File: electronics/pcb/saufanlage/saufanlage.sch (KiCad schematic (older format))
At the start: 36 parts

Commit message: Backup commit
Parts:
- removed C? (x4): C, symbol Device:C
- removed D?: D_Schottky, symbol Device:D_Schottky
- removed J?: Conn_02x20_Odd_Even, symbol Connector_Generic:Conn_02x20_Odd_Even
- removed J?: Screw_Terminal_01x02, symbol Connector:Screw_Terminal_01x02
- removed J? (x4): Conn_01x03_Male, symbol Connector:Conn_01x03_Male
- removed J?: Conn_01x02_Female, symbol Connector:Conn_01x02_Female
- removed J?: Conn_01x05_Male, symbol Connector:Conn_01x05_Male
- removed L?: L, symbol Device:L
- removed R? (x6): R, symbol Device:R
- removed SW?: SW_Push, symbol Switch:SW_Push
- removed U?: BD9G341EFJ, Package_SO:HTSOP-8-1EP_3.9x4.9mm_P1.27mm_EP2.4x3.2mm_ThermalVias, symbol Regulator_Switching:BD9G341EFJ
- added J1, J10, J11, J12, J16, J17, J3, J4: Conn_01x08_Male, Connector_PinHeader_2.54mm:PinHeader_1x08_P2.54mm_Vertical, symbol Connector:Conn_01x08_Male
- added J13: Conn_02x03_Odd_Even, Connector_PinHeader_2.54mm:PinHeader_2x03_P2.54mm_Vertical, symbol Connector_Generic:Conn_02x03_Odd_Even
- added J14: Conn_02x18_Odd_Even, Connector_PinHeader_2.54mm:PinHeader_2x18_P2.54mm_Vertical, symbol Connector_Generic:Conn_02x18_Odd_Even
- added J15, J27: Conn_01x10_Male, Connector_PinHeader_2.54mm:PinHeader_1x10_P2.54mm_Vertical, symbol Connector:Conn_01x10_Male
- added J18: Conn_01x04, Connector_PinHeader_2.54mm:PinHeader_1x04_P2.54mm_Vertical, symbol Connector_Generic:Conn_01x04
- added J2: Screw_Terminal_01x02, Connector_Phoenix_MC:PhoenixContact_MCV_1,5_2-G-3.81_1x02_P3.81mm_Vertical, symbol Connector:Screw_Terminal_01x02
- added J23, J24, J29, J30, J31, J32: Conn_01x15_Male, Connector_PinHeader_2.54mm:PinHeader_1x15_P2.54mm_Vertical, symbol Connector:Conn_01x15_Male
- added J7, J9: Conn_01x20_Male, Connector_PinHeader_2.54mm:PinHeader_1x20_P2.54mm_Vertical, symbol Connector:Conn_01x20_Male
- added PS1, PS2: LM2596, saufanlage:LM2596, symbol saufanlage:LM2596
- J19: renamed from J?; footprint (none) -> Connector_PinHeader_2.54mm:PinHeader_1x06_P2.54mm_Vertical
- J20: renamed from J?; footprint (none) -> Connector_PinHeader_2.54mm:PinHeader_1x07_P2.54mm_Vertical
- J21, J25, J26, J28: renamed from J?; footprint (none) -> Connector_PinHeader_2.54mm:PinHeader_1x03_P2.54mm_Vertical
- J22: renamed from J?; footprint (none) -> Connector_PinHeader_2.54mm:PinHeader_1x10_P2.54mm_Vertical
- J5, J6: renamed from J?; footprint (none) -> Connector_PinHeader_2.54mm:PinHeader_2x08_P2.54mm_Vertical
- J8: renamed from J?; footprint (none) -> Connector_PinHeader_2.54mm:PinHeader_2x20_P2.54mm_Vertical
- XA1: renamed from XA?; footprint (none) -> Arduino:Arduino_Mega2560_Shield
- XA2, XA3, XA4: renamed from XA?; footprint (none) -> Arduino:Arduino_Nano_Socket
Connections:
- net labels added: +3.3V, +3V3, +5V, +8V, DT1, DT2, DT3, DT4, Fingerprint, Flowmeter1, Flowmeter2, Flowmeter3, Flowmeter4, MEGA_D20_SDA, MEGA_D21_SCL, MEGA_RX0, MEGA_RX1, MEGA_RX2, MEGA_RX3, MEGA_RX4, MEGA_TX0, MEGA_TX1, MEGA_TX2, MISO, MOSI, M_3V3, M_5V, M_A0, M_A1, M_A10, M_A11, M_A12, M_A13, M_A14, M_A15, M_A2, M_A3, M_A4, M_A5, M_A6, M_A7, M_A8, M_A9, M_AREF, M_D10, M_D11, M_D12, M_D13, M_D2, M_D22, M_D23, M_D24, M_D25, M_D26, M_D27, M_D28, M_D29, M_D3, M_D30, M_D31, M_D32, M_D33, M_D34, M_D35, M_D36, M_D37, M_D38, M_D39, M_D4, M_D46, M_D47, M_D48, M_D49, M_D5, M_D50, M_D51, M_D52, M_D53, M_D6, M_D7, M_D8, M_D9, M_IORF, M_MISO, M_MOSI, M_RST1, M_RST2, M_SCK, M_SPI_5V, N1_3V3, N1_5V, N1_A0, N1_A1, N1_A2, N1_A3, N1_A6, N1_A7, N1_AREF, N1_D0, N1_D1, N1_D10, N1_D11, N1_D12, N1_D13, N1_D2_INT0, N1_D3_INT1, N1_D4, N1_D5, N1_D6, N1_D7, N1_D8, N1_D9, N1_RST1, N1_RST2, N2_3V3, N2_5V, N2_A0, N2_A1, N2_A2, N2_A3, N2_A6, N2_A7, N2_AREF, N2_D0, N2_D1, N2_D10, N2_D11, N2_D12, N2_D13, N2_D2_INT0, N2_D3_INT1, N2_D4, N2_D5, N2_D6, N2_D7, N2_D8, N2_D9, N2_RST1, N2_RST2, N3_3V3, N3_5V, N3_A0, N3_A1, N3_A2, N3_A3, N3_A6, N3_A7, N3_AREF, N3_D0, N3_D1, N3_D10, N3_D11, N3_D12, N3_D13, N3_D2_INT0, N3_D3_INT1, N3_D4, N3_D5, N3_D6, N3_D7, N3_D8, N3_D9, N3_RST1, N3_RST2, RELAIS1, RELAIS2, RELAIS3, RELAIS4, RELAIS5, RELAIS6, RPI_GPIO10, RPI_GPIO11, RPI_GPIO12, RPI_GPIO13, RPI_GPIO14, RPI_GPIO15, RPI_GPIO16, RPI_GPIO17, RPI_GPIO18, RPI_GPIO19, RPI_GPIO20, RPI_GPIO21, RPI_GPIO22, RPI_GPIO23, RPI_GPIO24, RPI_GPIO25, RPI_GPIO26, RPI_GPIO27, RPI_GPIO4, RPI_GPIO5, RPI_GPIO6, RPI_GPIO7, RPI_GPIO8, RPI_GPIO9, RPI_IDSC, RPI_IDSD, RST, SCK, SCK1, SCK2, SCK3, SCK4, UART_RX, UART_TX
- wire segments 249 -> 594
- no-connect marks 0 -> 1
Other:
- note added: "Fingerprint"
- note added: "Flowmeter"
- note added: "LED Matrix Connection"
- note added: "Mega Breakout"
- note added: "NFC"
- note added: "Nano #1 Breakout"
- note added: "Nano #2 Breakout"
- note added: "Nano #3 Breakout"
- note added: "Power Input"
- note added: "RPi Breakout"
- note added: "Scale1"
- note added: "Scale2"
- note removed: "Buck Converter"
- note removed: "Flowmeter-connection"
- note removed: "Raspberry - reset"
- moved on the sheet: J19, J20, J21, J22, J25, J26, J28, J5, J6, J8, XA1, XA2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

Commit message: More brainz updates
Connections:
- net N1_RST1: now also J23.13 (Pin_13); no longer J24.3 (Pin_3)
- net N1_RST2: now also J24.3 (Pin_3); no longer J23.13 (Pin_13)
- net N2_RST1: now also J29.13 (Pin_13); no longer J30.3 (Pin_3)
- net N2_RST2: now also J30.3 (Pin_3); no longer J29.13 (Pin_13)
- net N3_RST1: now also J31.13 (Pin_13); no longer J32.3 (Pin_3)
- net N3_RST2: now also J32.3 (Pin_3); no longer J31.13 (Pin_13)
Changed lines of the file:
@@
 	0    -1   -1   0
 $EndComp
-Text GLabel 12150 5300 2    50   Input ~ 0
-N1_RST1
 Text GLabel 12150 6200 2    50   Input ~ 0
 N1_A0
@@
 Text GLabel 12150 6300 2    50   Input ~ 0
 N1_AREF
-Text GLabel 11400 5300 0    50   Input ~ 0
-N1_RST2
 Wire Wire Line
 	11400 5200 11500 5200
@@
 	0    -1   -1   0
 $EndComp
-Text GLabel 16600 5300 2    50   Input ~ 0
-N2_RST1
 Text GLabel 16600 5700 2    50   Input ~ 0
 SCL
@@
 Text GLabel 16600 6300 2    50   Input ~ 0
 N2_AREF
-Text GLabel 15850 5300 0    50   Input ~ 0
-N2_RST2
 Wire Wire Line
 	15850 5200 15950 5200
@@
 	0    -1   -1   0
 $EndComp
-Text GLabel 21000 5300 2    50   Input ~ 0
-N3_RST1
 Text GLabel 21000 5500 2    50   Input ~ 0
 N3_A7
@@
 Text GLabel 21000 6300 2    50   Input ~ 0
 N3_AREF
-Text GLabel 20250 5300 0    50   Input ~ 0
-N3_RST2
 Wire Wire Line
 	20250 5200 20350 5200
@@
 Wire Wire Line
 	8150 8050 8200 8050
+Text GLabel 21000 5300 2    50   Input ~ 0
+N3_RST2
+Text GLabel 20250 5300 0    50   Input ~ 0
+N3_RST1
+Text GLabel 16600 5300 2    50   Input ~ 0
+N2_RST2
+Text GLabel 15850 5300 0    50   Input ~ 0
+N2_RST1
+Text GLabel 12150 5300 2    50   Input ~ 0
+N1_RST2
+Text GLabel 11400 5300 0    50   Input ~ 0
+N1_RST1
 $EndSCHEMATC

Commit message: Backup commit
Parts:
- removed J2: Screw_Terminal_01x02, Connector_Phoenix_MC:PhoenixContact_MCV_1,5_2-G-3.81_1x02_P3.81mm_Vertical, symbol Connector:Screw_Terminal_01x02
- added J2: PJ-031D, PJ-031D:CUI_PJ-031D, symbol saufanlage:PJ-031D
- added J33: Conn_7SegmentI2C, Connector_PinHeader_2.54mm:PinHeader_1x04_P2.54mm_Vertical, symbol Connector:Conn_01x04_Male
- J1: value Conn_01x08_Male -> Conn_GND
- J18: value Conn_01x04 -> Conn_Finger
- J19: value Conn_01x06_Female -> Conn_Relais
- J20: value Conn_01x07_Male -> Conn_NFC
- J21: value Conn_01x03_Male -> Conn_Flow1
- J22: value Conn_01x10_Male -> Conn_Scale1
- J25: value Conn_01x03_Male -> Conn_Flow2
- J26: value Conn_01x03_Male -> Conn_Flow3
- J27: value Conn_01x10_Male -> Conn_Scale2
- J28: value Conn_01x03_Male -> Conn_Flow4
- J3: value Conn_01x08_Male -> Conn_3V3
- J4: value Conn_01x08_Male -> Conn_5V
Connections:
- net +12V: now also J2.1 (PWR)
- net GND: now also J19.1 (Pin_1), J2.2 (SENSE), J2.3 (GND), J33.3 (Pin_3)
- net M_5V: now also J19.6 (Pin_6), J33.4 (Pin_4)
- net SCL: now also J33.1 (Pin_1)
- net SDA: now also J33.2 (Pin_2)
- net M_D10 renamed M_Flow1
- net M_D11 renamed M_Flow2
- net M_D12 renamed M_Flow3
- net M_D13 renamed M_Flow4
- removed net RELAIS1: J14.16 (Pin_16), J19.6 (Pin_6), XA1.D40
- net RELAIS2 renamed M_D40
- net M_D40: now also XA1.D40; no longer XA1.D41
- removed net RELAIS3: J14.14 (Pin_14), J19.4 (Pin_4), XA1.D42
- net RELAIS4 renamed M_D42
- net M_D42: now also XA1.D42; no longer XA1.D43
- removed net RELAIS5: J14.12 (Pin_12), J19.2 (Pin_2), XA1.D44
- removed net RELAIS6: J14.11 (Pin_11), J19.1 (Pin_1), XA1.D45
- new net M_D41: J14.16 (Pin_16), J19.4 (Pin_4), XA1.D41
- new net M_D43: J14.14 (Pin_14), J19.2 (Pin_2), XA1.D43
- new net M_D44: J14.11 (Pin_11), XA1.D44
- new net M_D45: J14.12 (Pin_12), XA1.D45
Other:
- note added: "I2C 7 Segment Display"

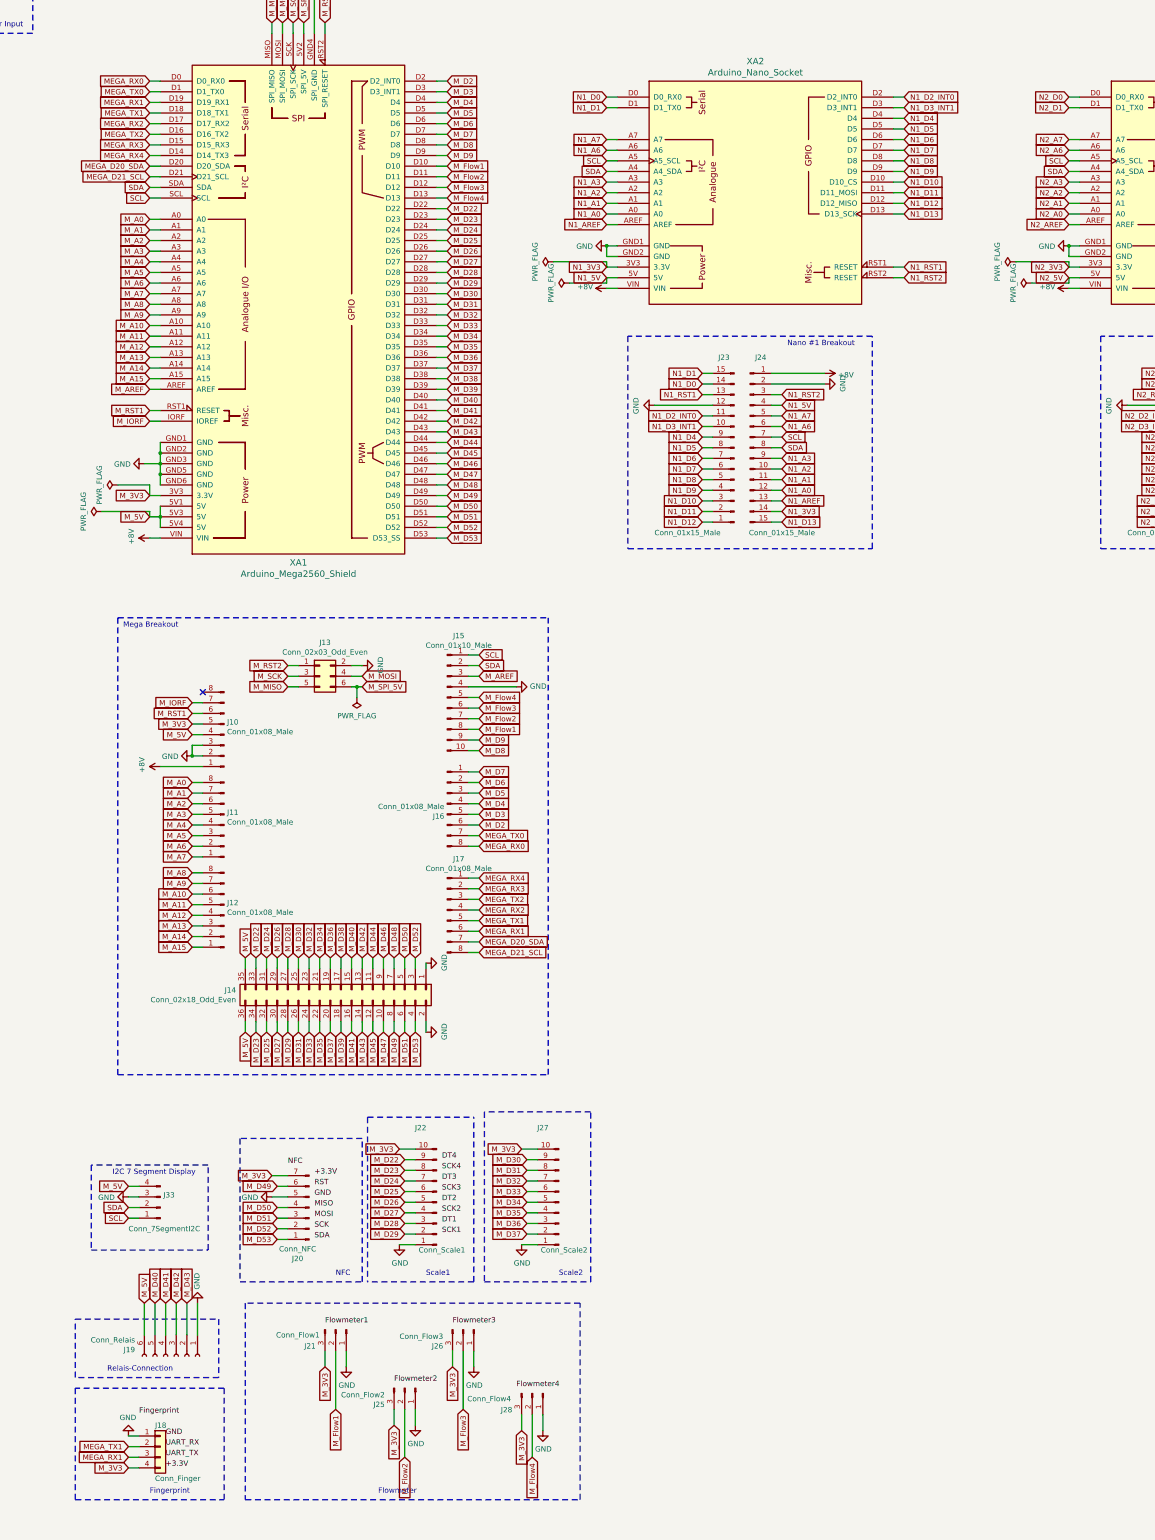
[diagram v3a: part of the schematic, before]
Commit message: Add fourth scale and temp sensor
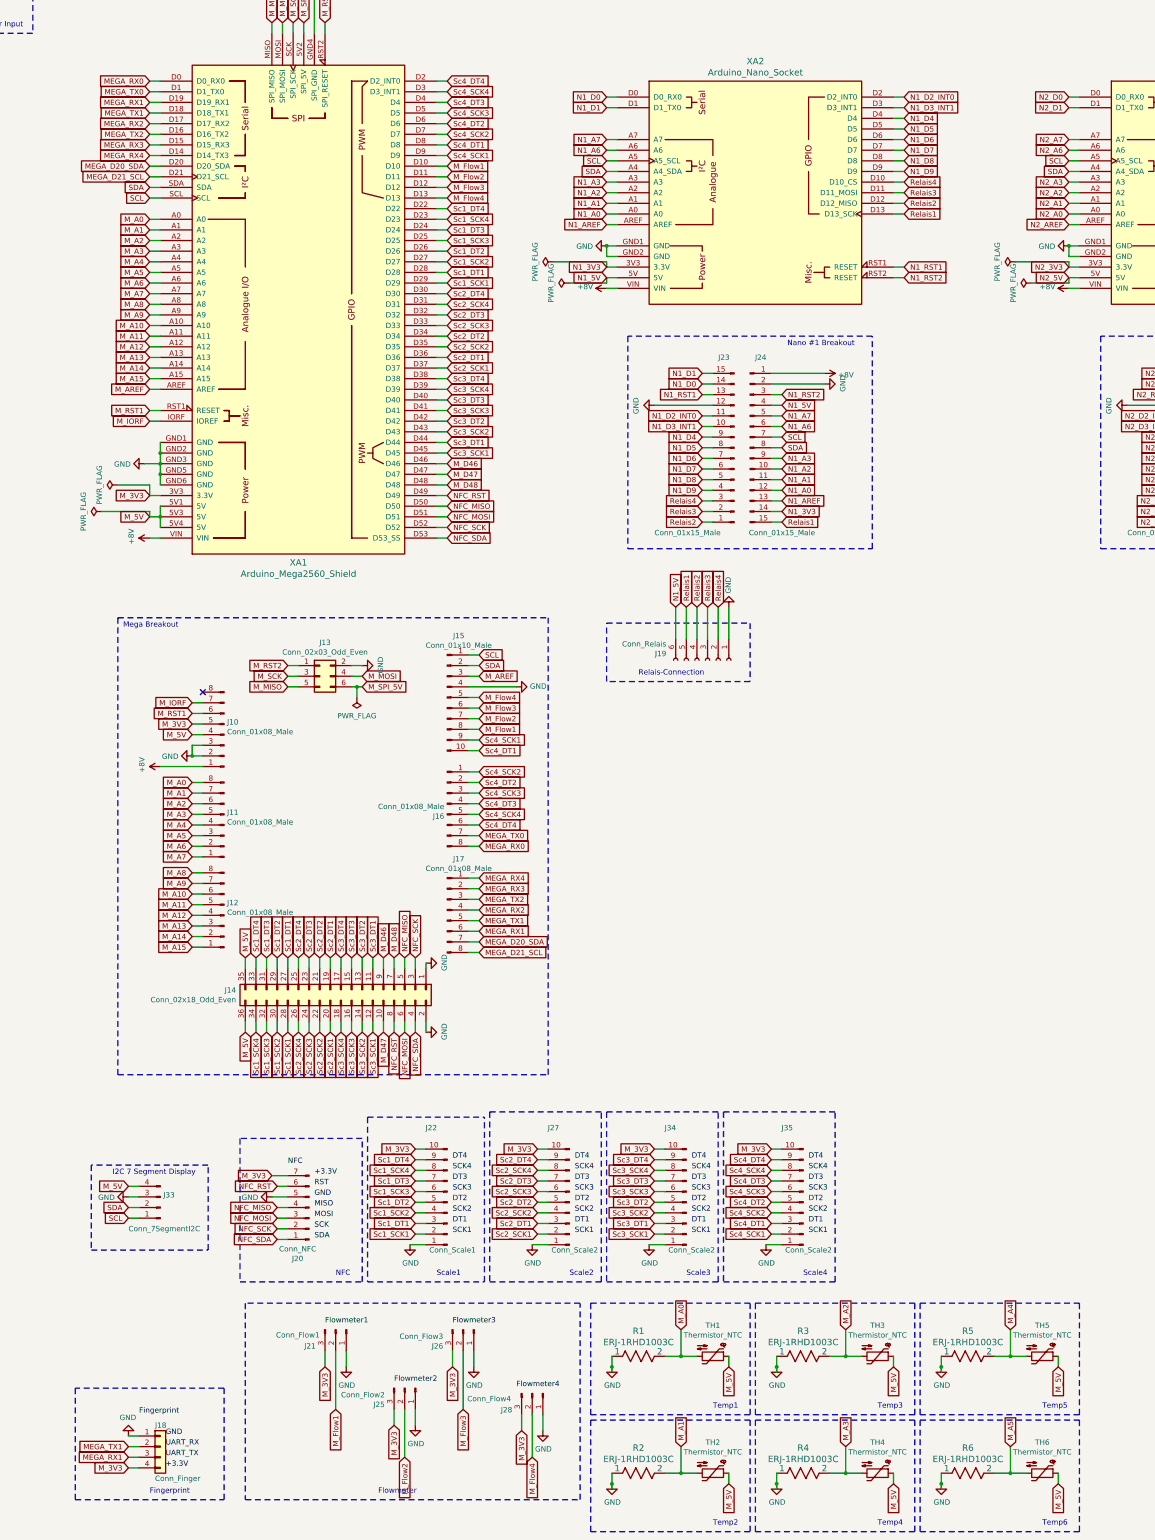
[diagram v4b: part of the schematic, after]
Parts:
- added J34, J35: Conn_Scale2, Connector_PinHeader_2.54mm:PinHeader_1x10_P2.54mm_Vertical, symbol Connector:Conn_01x10_Male
- added R1, R2, R3, R4, R5, R6: ERJ-1RHD1003C, saufanlage:ERJ-1RHD1003C, symbol 2020-02-06_21-37-09:ERJ-1RHD1003C
- added TH1, TH2, TH3, TH4, TH5, TH6: Thermistor_NTC, Connector_PinHeader_2.54mm:PinHeader_1x02_P2.54mm_Vertical, symbol Device:Thermistor_NTC
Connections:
- net GND: now also J34.1 (Pin_1), J35.1 (Pin_1), R1.1, R2.1, R3.1, R4.1, R5.1, R6.1
- net M_3V3: now also J34.10 (Pin_10), J35.10 (Pin_10)
- net M_5V: now also TH1.1, TH2.1, TH3.1, TH4.1, TH5.1, TH6.1; no longer J19.6 (Pin_6)
- net M_A0: now also R1.2, TH1.2
- net M_A1: now also R2.2, TH2.2
- net M_A2: now also R3.2, TH3.2
- net M_A3: now also R4.2, TH4.2
- net M_A4: now also R5.2, TH5.2
- net M_A5: now also R6.2, TH6.2
- net N1_5V: now also J19.6 (Pin_6)
- net M_D2 renamed Sc4_DT4
- net Sc4_DT4: now also J35.9 (Pin_9)
- net M_D22 renamed Sc1_DT4
- net M_D23 renamed Sc1_SCK4
- net M_D24 renamed Sc1_DT3
- net M_D25 renamed Sc1_SCK3
- net M_D26 renamed Sc1_DT2
- net M_D27 renamed Sc1_SCK2
- net M_D28 renamed Sc1_DT1
- net M_D29 renamed Sc1_SCK1
- net M_D3 renamed Sc4_SCK4
- net Sc4_SCK4: now also J35.8 (Pin_8)
- net M_D30 renamed Sc2_DT4
- net M_D31 renamed Sc2_SCK4
- net M_D32 renamed Sc2_DT3
- net M_D33 renamed Sc2_SCK3
- net M_D34 renamed Sc2_DT2
- net M_D35 renamed Sc2_SCK2
- net M_D36 renamed Sc2_DT1
- net M_D37 renamed Sc2_SCK1
- net M_D38 renamed Sc3_DT4
- net Sc3_DT4: now also J34.9 (Pin_9)
- net M_D39 renamed Sc3_SCK4
- net Sc3_SCK4: now also J34.8 (Pin_8)
- net M_D4 renamed Sc4_DT3
- net Sc4_DT3: now also J35.7 (Pin_7)
- net M_D40 renamed Sc3_DT3
- net Sc3_DT3: now also J34.7 (Pin_7); no longer J19.5 (Pin_5)
- net M_D41 renamed Sc3_SCK3
- net Sc3_SCK3: now also J34.6 (Pin_6); no longer J19.4 (Pin_4)
- net M_D42 renamed Sc3_DT2
- net Sc3_DT2: now also J34.5 (Pin_5); no longer J19.3 (Pin_3)
- net M_D43 renamed Sc3_SCK2
- net Sc3_SCK2: now also J34.4 (Pin_4); no longer J19.2 (Pin_2)
- net M_D44 renamed Sc3_DT1
- net Sc3_DT1: now also J34.3 (Pin_3)
- net M_D45 renamed Sc3_SCK1
- net Sc3_SCK1: now also J34.2 (Pin_2)
- net M_D49 renamed NFC_RST
- net M_D5 renamed Sc4_SCK3
- net Sc4_SCK3: now also J35.6 (Pin_6)
- net M_D50 renamed NFC_MISO
- net M_D51 renamed NFC_MOSI
- net M_D52 renamed NFC_SCK
- net M_D53 renamed NFC_SDA
- net M_D6 renamed Sc4_DT2
- net Sc4_DT2: now also J35.5 (Pin_5)
- net M_D7 renamed Sc4_SCK2
- net Sc4_SCK2: now also J35.4 (Pin_4)
- net M_D8 renamed Sc4_DT1
- net Sc4_DT1: now also J35.3 (Pin_3)
- net M_D9 renamed Sc4_SCK1
- net Sc4_SCK1: now also J35.2 (Pin_2)
- net N1_D10 renamed Relais4
- net Relais4: now also J19.2 (Pin_2)
- net N1_D11 renamed Relais3
- net Relais3: now also J19.3 (Pin_3)
- net N1_D12 renamed Relais2
- net Relais2: now also J19.4 (Pin_4)
- net N1_D13 renamed Relais1
- net Relais1: now also J19.5 (Pin_5)
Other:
- note added: "Scale3"
- note added: "Scale4"
- note added: "Temp1"
- note added: "Temp2"
- note added: "Temp3"
- note added: "Temp4"
- note added: "Temp5"
- note added: "Temp6"
- moved on the sheet: J19, J22, J27

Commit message: Backup commit
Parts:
- added C1, C10, C11, C12, C13, C14, C15, C16, C17, C2, C3, C4, C5, C6, C7, C8, C9: 08054D226MAT2A, Capacitor_SMD:C_0805_2012Metric_Pad1.15x1.40mm_HandSolder, symbol Device:C
- J27: renamed from J34; value Conn_Scale2 -> Conn_Scale3
- J31: renamed from J35; value Conn_Scale2 -> Conn_Scale4
- R1, R2, R3, R4, R5, R6: value ERJ-1RHD1003C -> ERJ-6RBD1003V; footprint saufanlage:ERJ-1RHD1003C -> Resistor_SMD:R_0805_2012Metric_Pad1.15x1.40mm_HandSolder; symbol 2020-02-06_21-37-09:ERJ-1RHD1003C -> 2020-02-06_21-37-09:ERJ-6RBD1003V
- renumbered J33 to J10, J18 to J11, J10 to J12, J11 to J13, J12 to J14, J20 to J15, J21 to J16, J13 to J17, J14 to J18, J25 to J19, J15 to J20, J16 to J21, J17 to J22, J22 to J23, J26 to J24, J28 to J25, J27 to J26, J19 to J28, J23 to J29, J24 to J30, J29 to J32, J30 to J33, J31 to J34, J32 to J35
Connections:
- net GND: now also C1.1, C10.1, C11.1, C12.1, C13.1, C14.1, C15.1, C16.1, C17.1, C2.1, C3.1, C4.1, C5.1, C6.1, C7.1, C8.1, C9.1; no longer J24.1 (Pin_1)
- net M_3V3: now also C1.2, C10.2, C13.2, C3.2, C4.2, C5.2, C6.2, C7.2, C8.2, C9.2
- net M_5V: now also C11.2, C12.2, C14.2, C15.2, C16.2, C17.2, C2.2
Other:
- moved on the sheet: J11, J16, J19, J24, J25
